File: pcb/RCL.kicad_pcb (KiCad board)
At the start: 2 copper layers, 52 x 52 mm, 86 parts, among them J1 USB_C_Receptacle, J2 Conn_01x02_Pin, J3 Conn_01x05_Pin, Q1 BSP613, Q2 AO3416A, Q3 AO3416A, Q4 AO3416A, SW1 SW_SPDT, SW2 SW_DIP_x02, SW3 SW_Push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

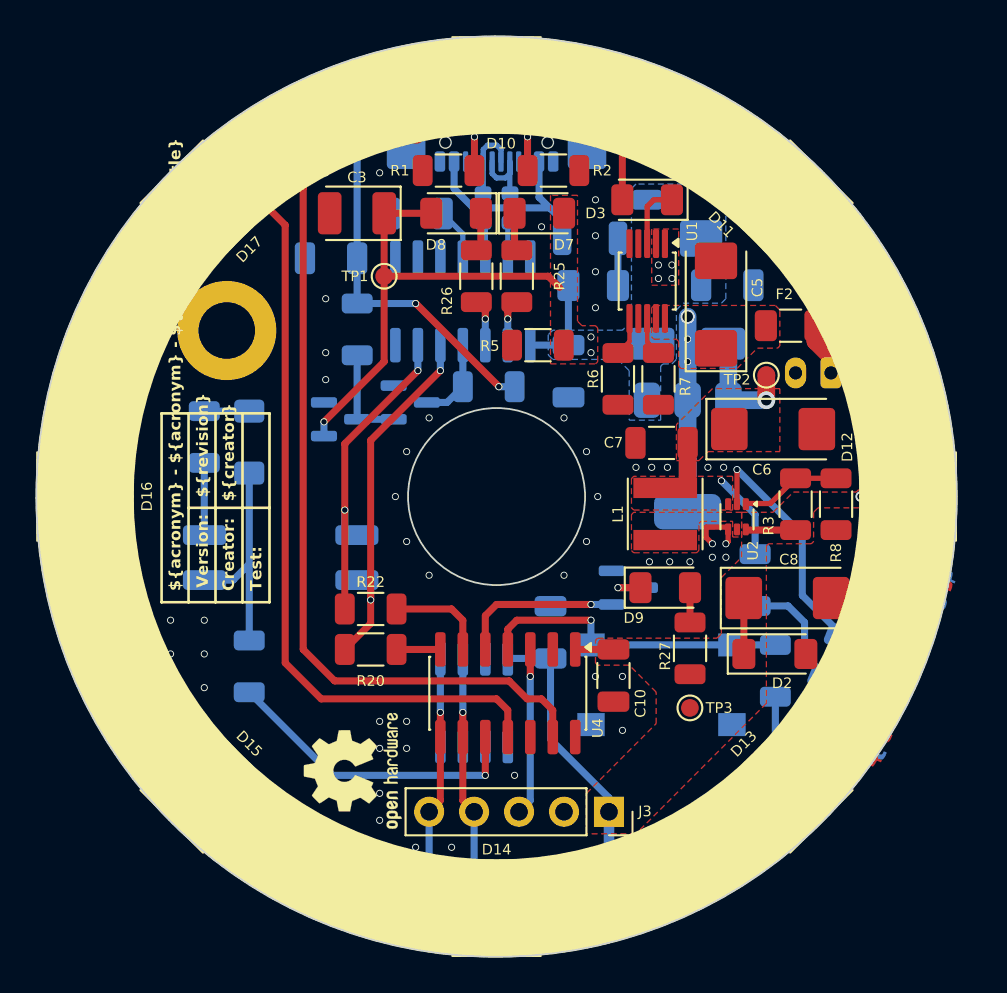
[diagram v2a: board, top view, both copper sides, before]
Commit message: Change MCP2221A to FT230X
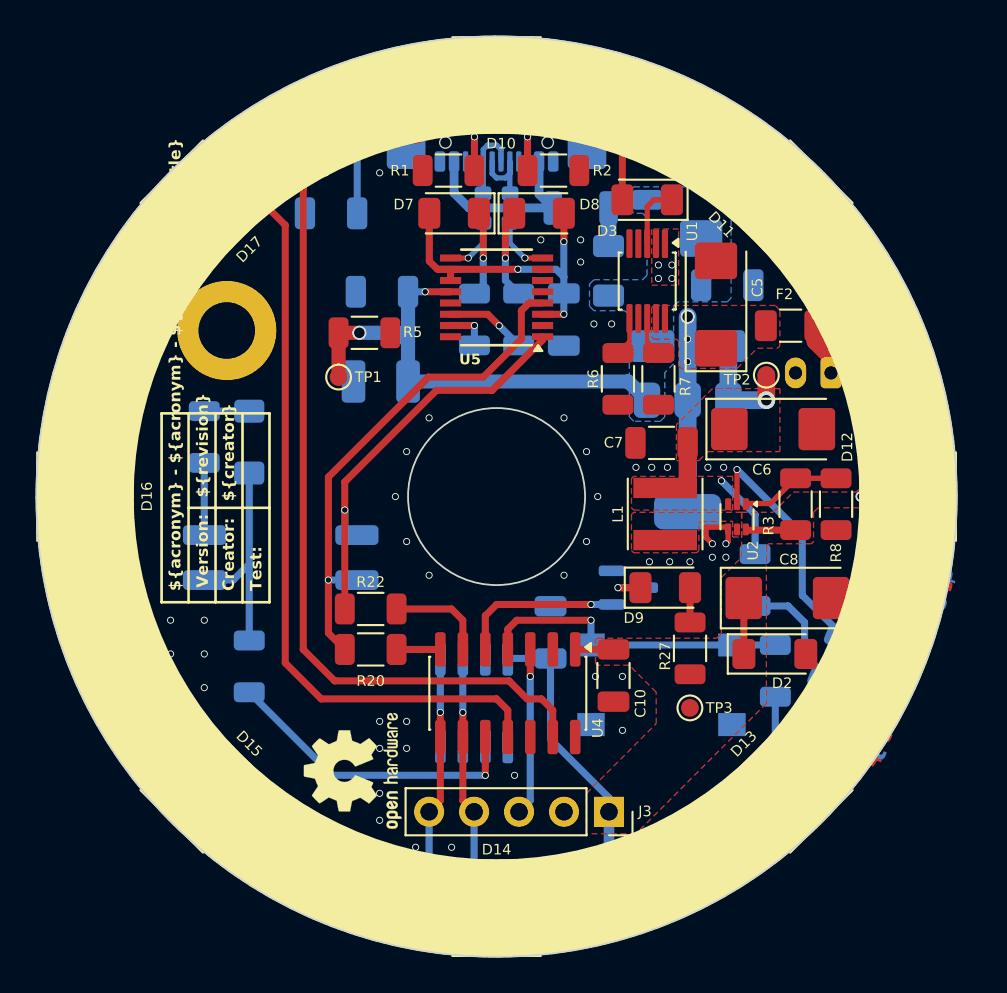
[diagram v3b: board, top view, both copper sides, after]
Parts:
- removed Q2, Q3: AO3416A, Package_TO_SOT_SMD:SOT-23
- removed R17, R23: 1k, Resistor_SMD:R_1206_3216Metric
- C3, R25, R26: moved to B.Cu
- U5: value MCP2221AxSL -> FT230XS; footprint Package_SO:SOIC-14_3.9x8.7mm_P1.27mm -> Package_SO:SSOP-16_3.9x4.9mm_P0.635mm; moved to F.Cu
- moved C4 11.5 mm to (150.5, 76.7), turned to 180 degrees
- moved C12 10.3 mm to (160.8, 78.3), turned to -90 degrees
- moved R5 9.82 mm to (149.5, 79.0), turned to 180 degrees
- moved C3 9.60 mm to (150.5, 81.8)
- moved TP1 6.25 mm to (148.1, 81.5)
- moved D7 4.82 mm to (154.6, 72.3), turned to 180 degrees
- moved D8 4.69 mm to (159.4, 72.3), turned to 0 degrees
- moved R25 3.42 mm to (155.8, 78.3)
- moved R26 3.42 mm to (158.3, 78.3)
- moved C11 2.54 mm to (147.7, 72.3)
- moved U5 1.92 mm to (157.0, 77.0), turned to 180 degrees
- moved FB1 1.79 mm to (161.8, 72.0)
- moved F1 1.20 mm to (163.3, 75.5), turned to -90 degrees
- moved D1 0.14 mm to (167.8, 79.8)
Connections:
- C12 pad 1: Net-(U5-VUSB) -> +3V3
- D7 pad 2: VBUS -> +3V3
- D8 pad 2: VBUS -> +3V3
- R20 pad 2: Net-(U5-URx) -> Net-(U5-RXD)
- R21 pad 2: Net-(U5-D+) -> Net-(U5-USBDP)
- R22 pad 2: Net-(U5-UTx) -> Net-(U5-TXD)
- R24 pad 2: Net-(U5-D-) -> Net-(U5-USBDM)
- R25 pad 2: Net-(U5-GP0) -> Net-(U5-CBUS0)
- R26 pad 2: Net-(U5-GP1) -> Net-(U5-CBUS1)
- SW2 pad 1: Net-(U5-UTx) -> Net-(U5-TXD)
- SW2 pad 2: Net-(U5-URx) -> Net-(U5-RXD)
- U5 pad 1: VBUS -> Net-(U5-TXD)
- U5 pad 10: unconnected-(U5-SCL-Pad10) -> +3V3
- U5 pad 11: Net-(U5-VUSB) -> +3V3
- U5 pad 12: Net-(U5-D-) -> VBUS
- U5 pad 13: Net-(U5-D+) -> GND
- U5 pad 14: GND -> Net-(U5-CBUS1)
- U5 pad 2: Net-(U5-GP0) -> unconnected-(U5-~{RTS}-Pad2)
- U5 pad 3: Net-(U5-GP1) -> +3V3
- U5 pad 4: Net-(Q2-D) -> Net-(U5-RXD)
- U5 pad 5: Net-(U5-URx) -> GND
- U5 pad 6: Net-(U5-UTx) -> unconnected-(U5-~{CTS}-Pad6)
- U5 pad 8: unconnected-(U5-GP3-Pad8) -> Net-(U5-USBDP)
- U5 pad 9: unconnected-(U5-SDA-Pad9) -> Net-(U5-USBDM)
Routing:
- net Net-(U5-RXD): track 0.00 -> 28.8 mm, vias 0 -> 1
- net Net-(U5-TXD): track 0.00 -> 23.8 mm, vias 0 -> 1
- net Net-(U5-URx): track 21.3 -> 0.00 mm, vias 2 -> 0
- net Net-(U5-UTx): track 18.5 -> 0.00 mm, vias 2 -> 0
- net +3V3: track 0.00 -> 18.2 mm, vias 0 -> 3
- net +5V: track 180.5 -> 164.6 mm, vias 12 -> 10
- net Net-(Q2-G): track 5.67 -> 0.00 mm
- net Net-(Q2-D): track 4.75 -> 0.00 mm
- net Net-(U5-CBUS1): track 0.00 -> 4.58 mm, vias 0 -> 1
- net VBUS: track 32.2 -> 28.0 mm, vias 7 -> 6
- net Net-(U5-USBDM): track 0.00 -> 3.53 mm, vias 0 -> 1
- net Net-(U5-USBDP): track 0.00 -> 3.35 mm, vias 0 -> 1
- net Net-(U5-VUSB): track 2.95 -> 0.00 mm
- net Net-(U5-GP1): track 2.64 -> 0.00 mm, vias 1 -> 0
- net Net-(U5-GP0): track 2.64 -> 0.00 mm, vias 1 -> 0
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
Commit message: Optimize +3V3 signal
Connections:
- net +3V3 renamed Net-(D7-A)
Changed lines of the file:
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@@
 	(net 70 "unconnected-(U5-CBUS3-Pad16)")
 	(net 71 "unconnected-(U5-CBUS2-Pad7)")
-	(net 72 "+3V3")
+	(net 72 "Net-(D7-A)")
 	(footprint "Package_TO_SOT_SMD:SOT-563"
 		(layer "F.Cu")
@@
 			(layers "F.Cu" "F.Mask" "F.Paste")
 			(roundrect_rratio 0.2)
-			(net 72 "+3V3")
+			(net 72 "Net-(D7-A)")
 			(pinfunction "A")
 			(pintype "passive")
@@
 			(layers "F.Cu" "F.Mask" "F.Paste")
 			(roundrect_rratio 0.2)
-			(net 72 "+3V3")
+			(net 72 "Net-(D7-A)")
 			(pinfunction "A")
 			(pintype "passive")
@@
 			(size 1.2 0.4)
 			(layers "F.Cu" "F.Mask" "F.Paste")
-			(net 72 "+3V3")
+			(net 72 "Net-(D7-A)")
 			(pinfunction "VCCIO")
 			(pintype "power_in")
@@
 			(size 1.2 0.4)
 			(layers "F.Cu" "F.Mask" "F.Paste")
-			(net 72 "+3V3")
+			(net 72 "Net-(D7-A)")
 			(pinfunction "3V3OUT")
 			(pintype "power_out")
@@
 			(size 1.2 0.4)
 			(layers "F.Cu" "F.Mask" "F.Paste")
-			(net 72 "+3V3")
+			(net 72 "Net-(D7-A)")
 			(pinfunction "~{RESET}")
 			(pintype "input")
@@
 			(layers "B.Cu" "B.Mask" "B.Paste")
 			(roundrect_rratio 0.217391)
-			(net 72 "+3V3")
+			(net 72 "Net-(D7-A)")
 			(pintype "passive")
 		)
